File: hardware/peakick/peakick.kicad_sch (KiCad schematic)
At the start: 36 parts, among them J1 CONN_161X16_SM_SQ_NOSILK, J2 QWIIC_RA, J3 CONN_12SM_SQ_NO_SILK, SW1 JS102011SAQN, U2 SAM-M10Q, U4 MMC5983MA, U5 BMP390, U6 ICM-42688-P, X2 JSTPH

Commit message: Doc updates
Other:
- note added: "I2C address 0x30"
- note added: "I2C address 0x42"
- note added: "I2C address 0x68"
- note added: "I2C address 0x77"
- moved on the sheet: C12, C13, U5

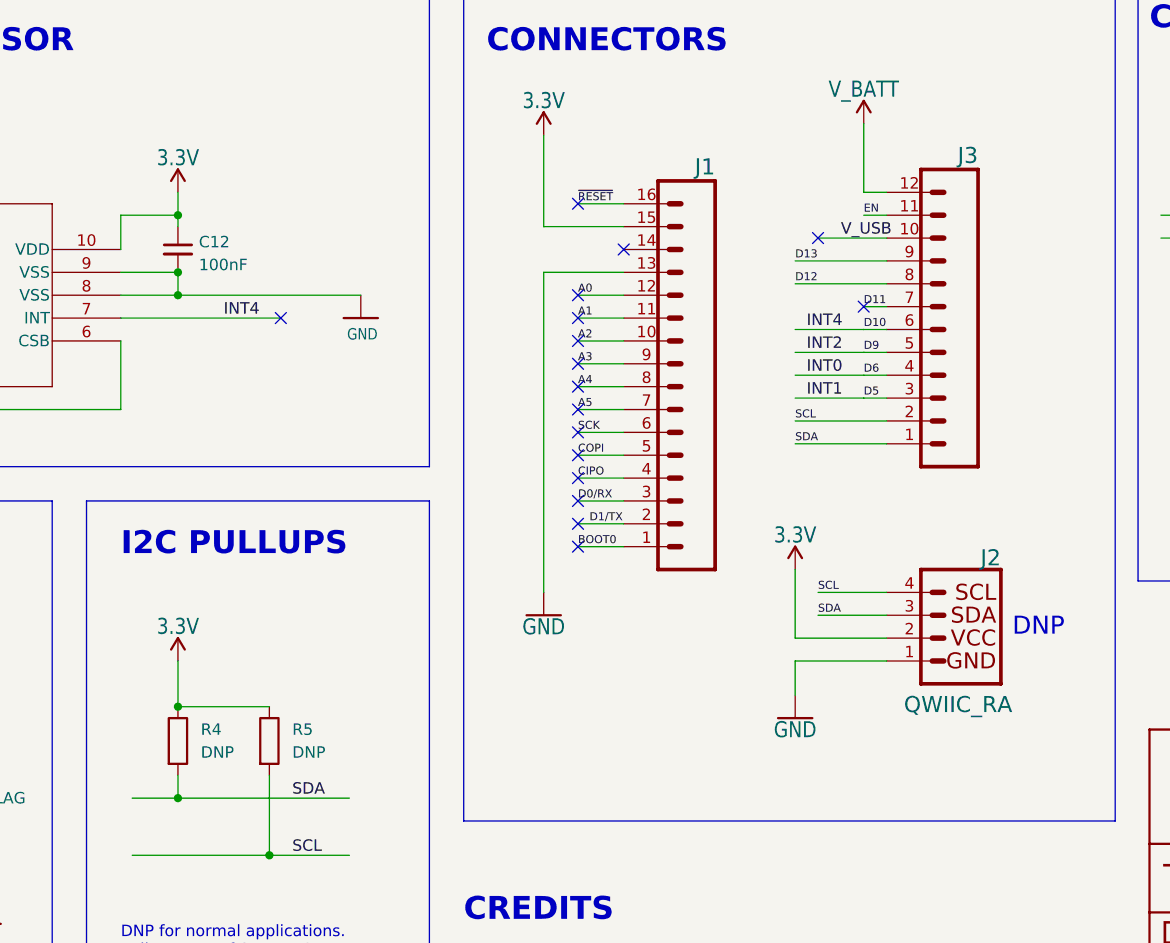
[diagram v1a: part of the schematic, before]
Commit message: Add Gerber, tweak BOM, remove solder mask around IMU pads
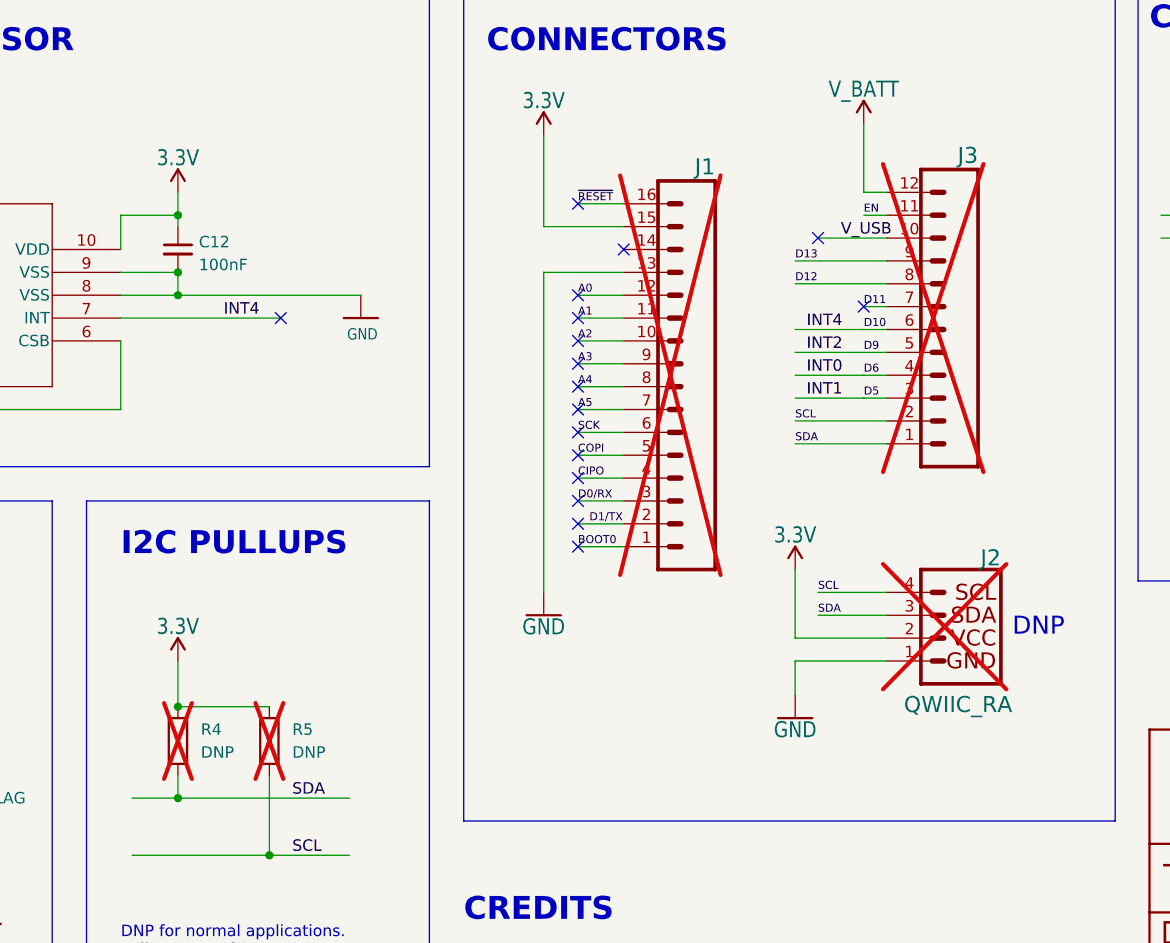
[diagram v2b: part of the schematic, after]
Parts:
- C1: PACKAGE (none) -> 0805
- C10, C11, C12, C13, C14, R10, R8: PACKAGE (none) -> 0603
- FD1, FD2, FD3, FD4, FRAME1, H1, H2, H3, H4, LOGO2: now left out of the parts list
- J1, J3: NOTES (none) -> DNP; now not fitted
- J2: now not fitted
- R4, R5: PACKAGE (none) -> 0603; now not fitted
- SW1: MANUFACTURER (none) -> CK Switches; MPN (none) -> JS102011SAQN
- U4: PACKAGE (none) -> LGA-16
- U5: PACKAGE (none) -> LGA-10
- U6: PACKAGE (none) -> LGA-14
- X2: MANUFACTURER (none) -> JST; MAXIMUM_PACKAGE_HEIGHT (none) -> 5.5mm

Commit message: Add pull-ups for I2C
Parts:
- R4, R5: value DNP -> 2K; NOTES 10K if SAM-M10 not installed -> (none); now fitted
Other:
- note added: "13 12 27 33 15 32 14"
- note added: "ESP32 Thing Plus C GPIO"
- note added: "Values valid for 400kbps operation"
- note removed: "DNP for normal applications. Pullups part of SAM-M10"
- moved on the sheet: J2, J3
